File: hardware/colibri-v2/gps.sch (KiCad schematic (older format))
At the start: 24 parts, among them CN7 82_MCX-50-0-17, Q17 IRLML6402TRPBF, U16 LEA-6S, U17 SM1411-5, U18 BGA825L6S

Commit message: Assigning footprints
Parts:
- removed L1: 330ohm/100MHz/300mA, symbol INDUCTOR
- added FB6: BEAD/330ohm/100MHz, Resistors_SMD:R_0805, symbol FB_SMT
- L2, L3: footprint (none) -> Resistors_SMD:R_0402
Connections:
- net at C65.2, C66.2, U16.6 (VCC): now also FB6.2
- net at C64.2, Q17.3 (D): now also FB6.1
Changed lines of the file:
@@
-$EndComp
-$Comp
-L INDUCTOR L1
-U 1 1 561881F0
-P 3250 3150
-F 0 "L1" V 3200 3150 50  0000 C CNN
-F 1 "330ohm/100MHz/300mA" V 3350 3150 50  0000 C CNN
-F 2 "" H 3250 3150 60  0001 C CNN
-F 3 "" H 3250 3150 60  0000 C CNN
-	1    3250 3150
-	0    -1   -1   0
 $EndComp
 $Comp
@@
 F 0 "L2" V 8650 3650 50  0000 C CNN
 F 1 "47nH/0A2/5%" V 8550 4050 50  0000 C CNN
-F 2 "" H 8600 4000 50  0001 C CNN
+F 2 "Resistors_SMD:R_0402" H 8600 4000 50  0001 C CNN
 F 3 "" H 8600 4000 50  0000 C CNN
 F 4 "Farnell" V 8600 4000 60  0001 C CNN "Provider"
@@
 F 0 "L3" V 8650 3850 50  0000 C CNN
 F 1 "5.6nH/800mA/±0.5nH/0402" V 8550 4200 50  0000 C CNN
-F 2 "" H 8600 4200 50  0001 C CNN
+F 2 "Resistors_SMD:R_0402" H 8600 4200 50  0001 C CNN
 F 3 "" H 8600 4200 50  0000 C CNN
 F 4 "Farnell" V 8600 4200 60  0001 C CNN "Provider"
@@
 	2750 2200 2750 3150
 Wire Wire Line
-	2750 3150 2950 3150
-Wire Wire Line
-	3550 3150 5050 3150
+	2750 3150 3050 3150
+Wire Wire Line
+	3450 3150 5050 3150
 Wire Wire Line
 	2750 1300 2750 1800
@@
 	4550 3000 4550 3150
 Connection ~ 4550 3150
+$Comp
+L FB_SMT FB6
+U 1 1 56CE3D74
+P 3250 3150
+F 0 "FB6" H 3250 3250 50  0000 C CNN
+F 1 "BEAD/330ohm/100MHz" H 3250 3100 50  0000 C CNN
+F 2 "Resistors_SMD:R_0805" H 3250 3050 30  0001 C CNN
+F 3 "" H 3300 3150 60  0000 C CNN
+F 4 "0805" H 3250 3150 25  0000 C CNN "SMT"
+F 5 "1515663" H 3250 3000 30  0001 C CNN "Part"
+F 6 "Farnell" H 3250 2950 30  0001 C CNN "Provider"
+	1    3250 3150
+	1    0    0    -1
+$EndComp
 $EndSCHEMATC

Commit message: Adding and assigning footprints
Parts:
- Q17: footprint (none) -> Sigmadrone:SOT23_IRLML6402
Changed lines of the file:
@@
 F 0 "Q17" H 2650 1850 50  0000 R CNN
 F 1 "IRLML6402TRPBF" V 2900 2300 50  0000 R CNN
-F 2 "" H 2850 2100 29  0001 C CNN
+F 2 "Sigmadrone:SOT23_IRLML6402" H 2850 2100 29  0001 C CNN
 F 3 "" H 2650 2000 60  0000 C CNN
 	1    2650 2000

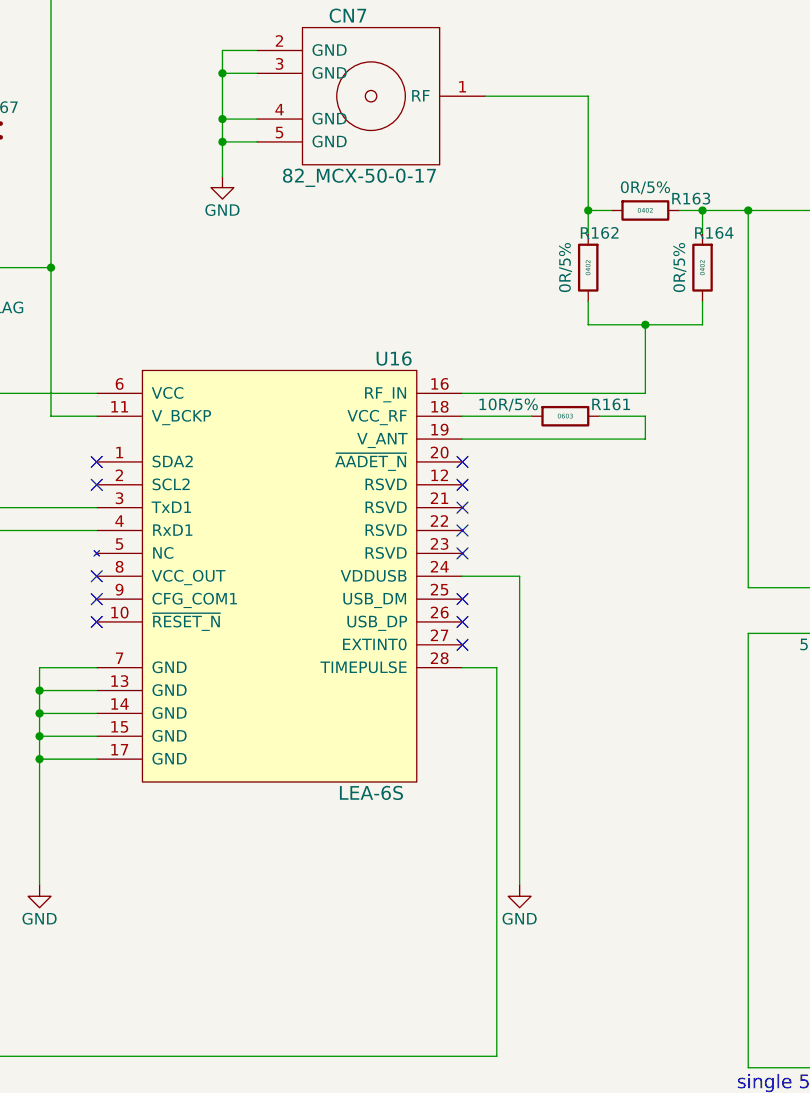
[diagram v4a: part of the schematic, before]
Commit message: Added footprints
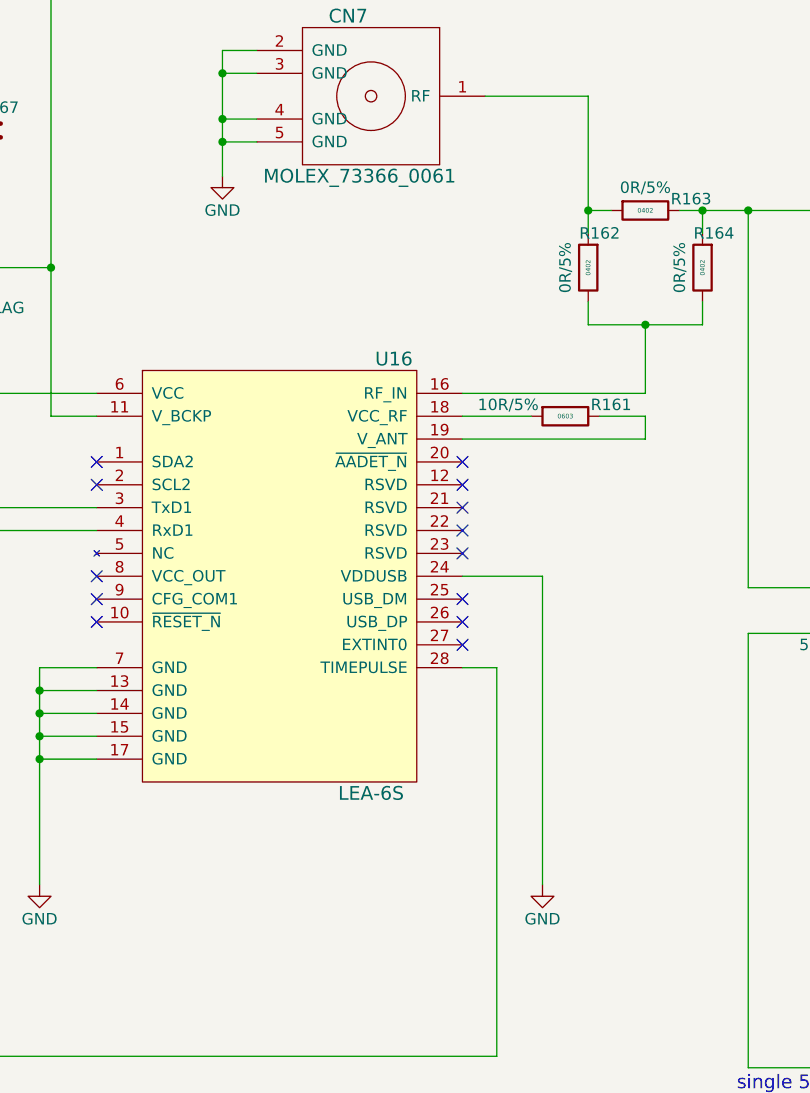
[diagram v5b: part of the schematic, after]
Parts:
- CN7: value 82_MCX-50-0-17 -> MOLEX_73366_0061; footprint (none) -> Sigmadrone:MOLEX_73366_0061
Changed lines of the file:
@@
 L GND #PWR0210
 U 1 1 5618714A
-P 6900 5300
-F 0 "#PWR0210" H 6900 5050 50  0001 C CNN
-F 1 "GND" H 6900 5150 50  0000 C CNN
-F 2 "" H 6900 5300 60  0000 C CNN
-F 3 "" H 6900 5300 60  0000 C CNN
-	1    6900 5300
+P 7000 5300
+F 0 "#PWR0210" H 7000 5050 50  0001 C CNN
+F 1 "GND" H 7000 5150 50  0000 C CNN
+F 2 "" H 7000 5300 60  0000 C CNN
+F 3 "" H 7000 5300 60  0000 C CNN
+	1    7000 5300
 	1    0    0    -1
 $EndComp
@@
 P 6250 1850
 F 0 "CN7" H 6350 2200 60  0000 C CNN
-F 1 "82_MCX-50-0-17" H 6300 1500 60  0000 C CNN
-F 2 "" H 6250 1850 60  0001 C CNN
+F 1 "MOLEX_73366_0061" H 6300 1500 60  0000 C CNN
+F 2 "Sigmadrone:MOLEX_73366_0061" H 6250 1850 60  0001 C CNN
 F 3 "" H 6250 1850 60  0000 C CNN
 F 4 "Farnell" H 6250 1850 60  0001 C CNN "Provider"
@@
 Connection ~ 4800 4750
 Wire Wire Line
-	6650 3950 6900 3950
+	6650 3950 7000 3950
 Wire Wire Line
 	2750 2200 2750 3150
@@
 Connection ~ 7450 2850
 Wire Wire Line
-	6900 3950 6900 5300
+	7000 3950 7000 5300
 Wire Wire Line
 	6650 3250 6950 3250

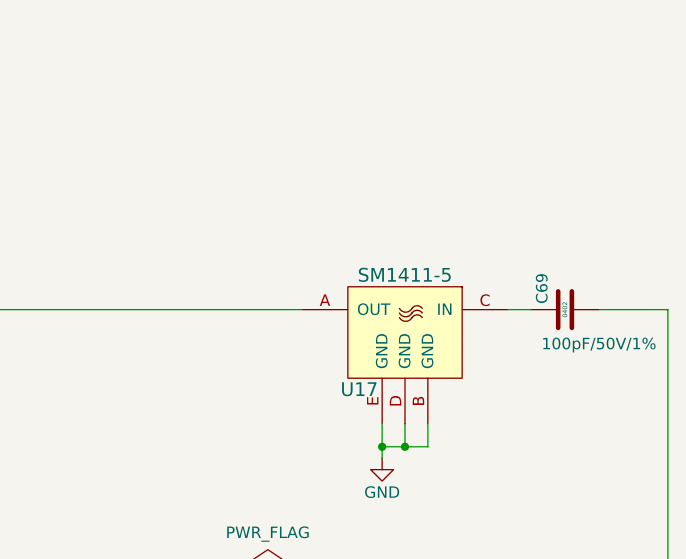
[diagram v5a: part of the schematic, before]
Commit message: Added footprints
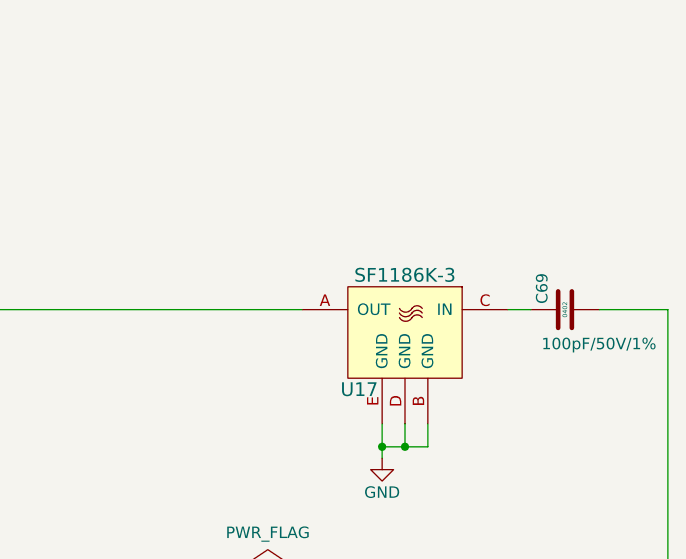
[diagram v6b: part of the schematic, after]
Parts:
- U17: value SM1411-5 -> SF1186K-3; footprint (none) -> Sigmadrone:SF1186K-3; Part (none) -> 583-1182-1-ND; Provider (none) -> Digikey
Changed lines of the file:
@@
 P 9750 2450
 F 0 "U17" H 9950 2200 60  0000 C CNN
-F 1 "SM1411-5" H 9750 2700 60  0000 C CNN
-F 2 "" H 9750 2400 60  0001 C CNN
+F 1 "SF1186K-3" H 9750 2700 60  0000 C CNN
+F 2 "Sigmadrone:SF1186K-3" H 9750 2400 60  0001 C CNN
 F 3 "" H 9750 2400 60  0000 C CNN
+F 4 "583-1182-1-ND" H 9750 2450 60  0001 C CNN "Part"
+F 5 "Digikey" H 9750 2450 60  0001 C CNN "Provider"
 	1    9750 2450
 	-1   0    0    -1

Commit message: Assigned footprints
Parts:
- U16: footprint (none) -> Sigmadrone:LEA-6
- U18: footprint (none) -> Sigmadrone:TSLP-6-3
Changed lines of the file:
@@
 F 0 "U16" H 6350 4900 60  0000 C CNN
 F 1 "LEA-6S" H 6250 3000 60  0000 C CNN
-F 2 "" H 5700 4050 60  0001 C CNN
+F 2 "Sigmadrone:LEA-6" H 5700 4050 60  0001 C CNN
 F 3 "" H 5700 4050 60  0000 C CNN
 	1    5850 3950
@@
 F 0 "U18" H 10300 4650 60  0000 C CNN
 F 1 "BGA825L6S" H 10050 3950 60  0000 C CNN
-F 2 "" H 10050 4250 60  0001 C CNN
+F 2 "Sigmadrone:TSLP-6-3" H 10050 4250 60  0001 C CNN
 F 3 "" H 10050 4250 60  0000 C CNN
 F 4 "Digikey" H 10050 3850 60  0001 C CNN "Provider"
